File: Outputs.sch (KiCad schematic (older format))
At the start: 6 parts, among them Q7 MOSFET-N-SOT223

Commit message: Redesigned schematics and board
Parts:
- removed Q7: MOSFET-N-SOT223, symbol PIP-3104
- added Q7: VND14NV04, symbol MOSFET_N
- R53: renamed from R44; value 470 -> 2.4k
- renumbered D29 to D30, D30 to D31, D28 to D32, R43 to R54
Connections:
- net labels removed: FP-LED-5v
- wire segments 6 -> 9
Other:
- note added: "Fuel Pump Relay Output"
- moved on the sheet: D30, D31, D32, R53, R54
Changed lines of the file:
@@
-EESchema Schematic File Version 2  date Thu 19 Jan 2012 12:17:41 AM EST
+EESchema Schematic File Version 2  date Fri 20 Jan 2012 02:23:37 PM EST
 LIBS:power
 LIBS:device
@@
 Sheet 2 7
 Title "Outputs"
-Date "19 jan 2012"
+Date "20 jan 2012"
 Rev "A"
 Comp "Jaguar Board for FreeEMS"
@@
 Comment4 ""
 $EndDescr
-Connection ~ 7300 2000
 $Comp
-L DIODE D30
+L MOSFET_N Q7
+U 1 1 4F19BBF5
+P 6250 3500
+F 0 "Q7" H 6260 3670 60  0000 R CNN
+F 1 "VND14NV04" H 6260 3350 60  0000 R CNN
+	1    6250 3500
+	1    0    0    -1
+$EndComp
+Connection ~ 4700 2700
+Wire Wire Line
+	4700 3100 4700 2700
+Connection ~ 6500 3100
+Wire Wire Line
+	6000 3100 6500 3100
+Connection ~ 6000 3100
+Connection ~ 5600 3100
+Connection ~ 4700 3100
+Connection ~ 5200 3100
+Connection ~ 5250 3500
+Connection ~ 5750 3500
+Connection ~ 6050 3500
+Connection ~ 6350 3700
+Connection ~ 6350 3300
+Connection ~ 6500 3300
+Connection ~ 6500 2700
+Wire Wire Line
+	6350 3700 6350 3900
+Wire Wire Line
+	6350 3900 6250 3900
+Wire Wire Line
+	5750 3500 6050 3500
+Wire Wire Line
+	5250 3500 5100 3500
+Wire Wire Line
+	6350 3300 6650 3300
+Wire Wire Line
+	6500 3100 6500 3300
+Wire Wire Line
+	4600 2700 6650 2700
+Text Notes 5500 4300 0    40   ~ 0
+Fuel Pump Relay Output
+$Comp
+L DIODE D31
 U 1 1 4F1784DB
-P 7100 2000
-F 0 "D30" H 7100 2100 40  0000 C CNN
-F 1 "1N4148" H 7100 1900 40  0000 C CNN
-	1    7100 2000
+P 5800 3100
+F 0 "D31" H 5800 3200 40  0000 C CNN
+F 1 "1N4148" H 5800 3000 40  0000 C CNN
+	1    5800 3100
 	1    0    0    -1
 $EndComp
 $Comp
-L PIP-3104 Q7
-U 1 1 4F14621B
-P 3050 2450
-F 0 "Q7" H 3060 2620 60  0000 R CNN
-F 1 "MOSFET-N-SOT223" H 3060 2300 60  0000 R CNN
-	1    3050 2450
-	1    0    0    -1
-$EndComp
-Connection ~ 6900 2000
-Text HLabel 7300 2000 2    60   Output ~ 0
-Relay_Negative
-Text HLabel 6000 2000 0    40   Input ~ 0
-FP-LED-5v
-Connection ~ 6000 2000
-Connection ~ 6500 2000
-$Comp
-L LED D29
+L LED D30
 U 1 1 4F1384E1
-P 6700 2000
-F 0 "D29" H 6700 2100 50  0000 C CNN
-F 1 "LED" H 6700 1900 50  0000 C CNN
-	1    6700 2000
+P 5400 3100
+F 0 "D30" H 5400 3200 40  0000 C CNN
+F 1 "LED" H 5400 3000 40  0000 C CNN
+	1    5400 3100
 	1    0    0    -1
 $EndComp
 $Comp
-L R R44
+L R R53
 U 1 1 4F1384D7
-P 6250 2000
-F 0 "R44" V 6330 2000 50  0000 C CNN
-F 1 "470" V 6250 2000 50  0000 C CNN
-	1    6250 2000
+P 4950 3100
+F 0 "R53" V 5030 3100 40  0000 C CNN
+F 1 "2.4k" V 4950 3100 40  0000 C CNN
+	1    4950 3100
 	0    1    1    0
 $EndComp
-Connection ~ 2050 2450
-Connection ~ 2550 2450
-Connection ~ 2850 2450
-Connection ~ 3150 2650
-Connection ~ 3150 2250
-Connection ~ 3300 2250
-Connection ~ 3300 1850
-Wire Wire Line
-	3450 1850 3100 1850
-Wire Wire Line
-	3150 2650 3150 2850
-Wire Wire Line
-	3150 2850 3050 2850
-Wire Wire Line
-	2550 2450 2850 2450
-Wire Wire Line
-	2050 2450 1900 2450
-Wire Wire Line
-	3150 2250 3450 2250
-Text HLabel 1900 2450 0    60   Input ~ 0
+Text HLabel 5100 3500 0    40   Input ~ 0
 PA7
-Text HLabel 3050 2850 0    60   Input ~ 0
+Text HLabel 6250 3900 0    40   Input ~ 0
 GND
-Text HLabel 3450 2250 2    60   Output ~ 0
+Text HLabel 6650 3300 2    40   Output ~ 0
 Relay_Negative
-Text HLabel 3450 1850 2    60   Output ~ 0
+Text HLabel 6650 2700 2    40   Output ~ 0
 Relay_Positive
-Text HLabel 3100 1850 0    60   Input ~ 0
+Text HLabel 4600 2700 0    40   Input ~ 0
 12vdc-switched-relay
 $Comp
-L DIODE D28
+L DIODE D32
 U 1 1 4F074524
-P 3300 2050
-F 0 "D28" H 3300 2150 40  0000 C CNN
-F 1 "1N4004" H 3300 1950 40  0000 C CNN
-	1    3300 2050
+P 6500 2900
+F 0 "D32" H 6500 3000 40  0000 C CNN
+F 1 "1N4004" H 6500 2800 40  0000 C CNN
+	1    6500 2900
 	0    -1   -1   0
 $EndComp
 $Comp
-L R R43
+L R R54
 U 1 1 4F0744B6
-P 2300 2450
-F 0 "R43" V 2380 2450 50  0000 C CNN
-F 1 "1k" V 2300 2450 50  0000 C CNN
-	1    2300 2450
+P 5500 3500
+F 0 "R54" V 5580 3500 40  0000 C CNN
+F 1 "1k" V 5500 3500 40  0000 C CNN
+	1    5500 3500
 	0    1    1    0
 $EndComp

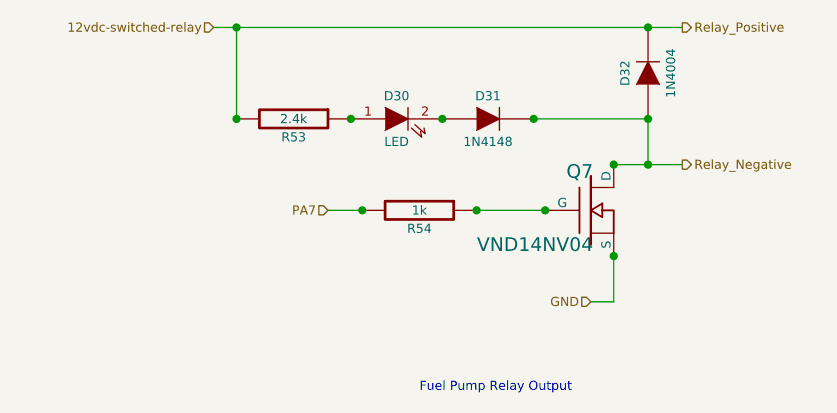
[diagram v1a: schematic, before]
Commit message: Updated Schematics, created new PDF, completed board layout and routing
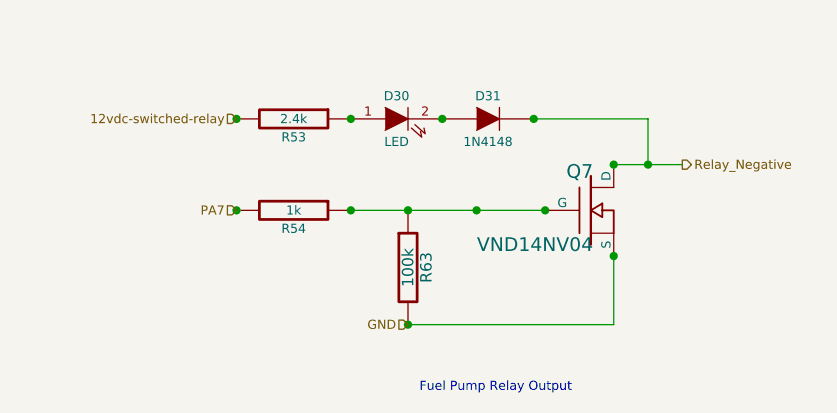
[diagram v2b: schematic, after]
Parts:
- removed D32: 1N4004, symbol DIODE
- added R63: 100k, symbol R
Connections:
- net GND: now also R63.2
- net at Q7.G, R54.1: now also R63.1
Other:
- moved on the sheet: R54
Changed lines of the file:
@@
-EESchema Schematic File Version 2  date Fri 20 Jan 2012 02:23:37 PM EST
+EESchema Schematic File Version 2  date Sun 22 Jan 2012 12:58:37 AM EST
 LIBS:power
 LIBS:device
@@
 Sheet 2 7
 Title "Outputs"
-Date "20 jan 2012"
+Date "22 jan 2012"
 Rev "A"
 Comp "Jaguar Board for FreeEMS"
@@
 Comment4 ""
 $EndDescr
+Connection ~ 4700 3500
+Connection ~ 5200 3500
+Connection ~ 5450 3500
+Connection ~ 5450 4000
+Wire Wire Line
+	6350 3700 6350 4000
+Wire Wire Line
+	6350 4000 5450 4000
+Wire Wire Line
+	5200 3500 6050 3500
+Wire Wire Line
+	6000 3100 6500 3100
+Connection ~ 6000 3100
+Connection ~ 5600 3100
+Connection ~ 4700 3100
+Connection ~ 5200 3100
+Connection ~ 5750 3500
+Connection ~ 6050 3500
+Connection ~ 6350 3700
+Connection ~ 6350 3300
+Connection ~ 6500 3300
+Wire Wire Line
+	6350 3300 6650 3300
+Wire Wire Line
+	6500 3100 6500 3300
+$Comp
+L R R63
+U 1 1 4F1AF0F6
+P 5450 3750
+F 0 "R63" V 5530 3750 50  0000 C CNN
+F 1 "100k" V 5450 3750 50  0000 C CNN
+	1    5450 3750
+	1    0    0    -1
+$EndComp
 $Comp
 L MOSFET_N Q7
@@
 	1    0    0    -1
 $EndComp
-Connection ~ 4700 2700
-Wire Wire Line
-	4700 3100 4700 2700
-Connection ~ 6500 3100
-Wire Wire Line
-	6000 3100 6500 3100
-Connection ~ 6000 3100
-Connection ~ 5600 3100
-Connection ~ 4700 3100
-Connection ~ 5200 3100
-Connection ~ 5250 3500
-Connection ~ 5750 3500
-Connection ~ 6050 3500
-Connection ~ 6350 3700
-Connection ~ 6350 3300
-Connection ~ 6500 3300
-Connection ~ 6500 2700
-Wire Wire Line
-	6350 3700 6350 3900
-Wire Wire Line
-	6350 3900 6250 3900
-Wire Wire Line
-	5750 3500 6050 3500
-Wire Wire Line
-	5250 3500 5100 3500
-Wire Wire Line
-	6350 3300 6650 3300
-Wire Wire Line
-	6500 3100 6500 3300
-Wire Wire Line
-	4600 2700 6650 2700
 Text Notes 5500 4300 0    40   ~ 0
 Fuel Pump Relay Output
@@
 	0    1    1    0
 $EndComp
-Text HLabel 5100 3500 0    40   Input ~ 0
+Text HLabel 4700 3500 0    40   Input ~ 0
 PA7
-Text HLabel 6250 3900 0    40   Input ~ 0
+Text HLabel 5450 4000 0    40   Input ~ 0
 GND
 Text HLabel 6650 3300 2    40   Output ~ 0
 Relay_Negative
-Text HLabel 6650 2700 2    40   Output ~ 0
-Relay_Positive
-Text HLabel 4600 2700 0    40   Input ~ 0
+Text HLabel 4700 3100 0    40   Input ~ 0
 12vdc-switched-relay
-$Comp
-L DIODE D32
-U 1 1 4F074524
-P 6500 2900
-F 0 "D32" H 6500 3000 40  0000 C CNN
-F 1 "1N4004" H 6500 2800 40  0000 C CNN
-	1    6500 2900
-	0    -1   -1   0
-$EndComp
 $Comp
 L R R54
 U 1 1 4F0744B6
-P 5500 3500
-F 0 "R54" V 5580 3500 40  0000 C CNN
-F 1 "1k" V 5500 3500 40  0000 C CNN
-	1    5500 3500
+P 4950 3500
+F 0 "R54" V 5030 3500 40  0000 C CNN
+F 1 "1k" V 4950 3500 40  0000 C CNN
+	1    4950 3500
 	0    1    1    0
 $EndComp

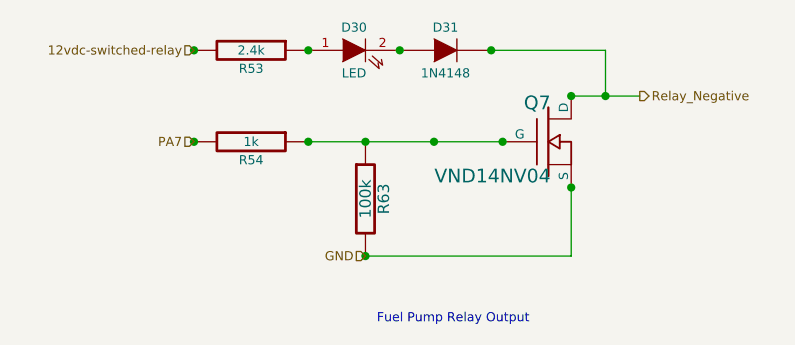
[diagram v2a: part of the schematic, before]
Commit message: Modified: schematics to correct errors
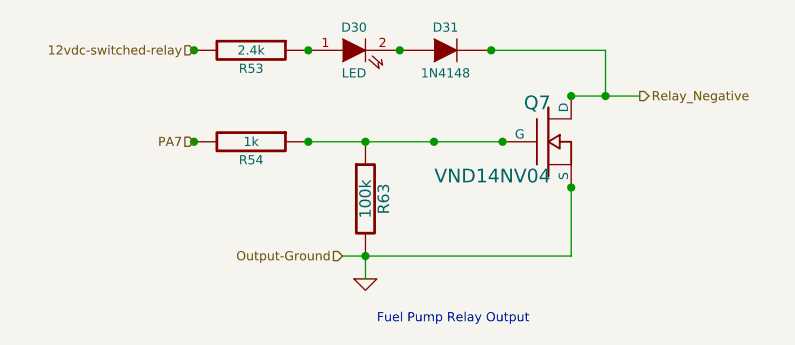
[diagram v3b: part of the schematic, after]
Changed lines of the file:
@@
-EESchema Schematic File Version 2  date Sun 22 Jan 2012 12:58:37 AM EST
+EESchema Schematic File Version 2  date Sun 22 Jan 2012 05:59:51 PM EST
 LIBS:power
 LIBS:device
@@
 Comment4 ""
 $EndDescr
-Connection ~ 4700 3500
-Connection ~ 5200 3500
-Connection ~ 5450 3500
-Connection ~ 5450 4000
+$Comp
+L GND #PWR56
+U 1 1 4F1C4528
+P 5450 4100
+F 0 "#PWR56" H 5450 4100 30  0001 C CNN
+F 1 "GND" H 5450 4030 30  0001 C CNN
+	1    5450 4100
+	1    0    0    -1
+$EndComp
 Wire Wire Line
-	6350 3700 6350 4000
+	5450 4100 5450 4000
 Wire Wire Line
-	6350 4000 5450 4000
+	6500 3300 6500 3100
+Wire Wire Line
+	6350 3300 6650 3300
+Connection ~ 6500 3300
+Connection ~ 6350 3300
+Connection ~ 6350 3700
+Connection ~ 6050 3500
+Connection ~ 5750 3500
+Connection ~ 5200 3100
+Connection ~ 4700 3100
+Connection ~ 5600 3100
+Connection ~ 6000 3100
+Wire Wire Line
+	6500 3100 6000 3100
 Wire Wire Line
 	5200 3500 6050 3500
 Wire Wire Line
-	6000 3100 6500 3100
-Connection ~ 6000 3100
-Connection ~ 5600 3100
-Connection ~ 4700 3100
-Connection ~ 5200 3100
-Connection ~ 5750 3500
-Connection ~ 6050 3500
-Connection ~ 6350 3700
-Connection ~ 6350 3300
-Connection ~ 6500 3300
+	6350 3700 6350 4000
+Connection ~ 5450 4000
+Connection ~ 5450 3500
+Connection ~ 5200 3500
+Connection ~ 4700 3500
 Wire Wire Line
-	6350 3300 6650 3300
-Wire Wire Line
-	6500 3100 6500 3300
+	6350 4000 5350 4000
+Text HLabel 5350 4000 0    40   Input ~ 0
+Output-Ground
 $Comp
 L R R63
@@
 Text HLabel 4700 3500 0    40   Input ~ 0
 PA7
-Text HLabel 5450 4000 0    40   Input ~ 0
-GND
 Text HLabel 6650 3300 2    40   Output ~ 0
 Relay_Negative

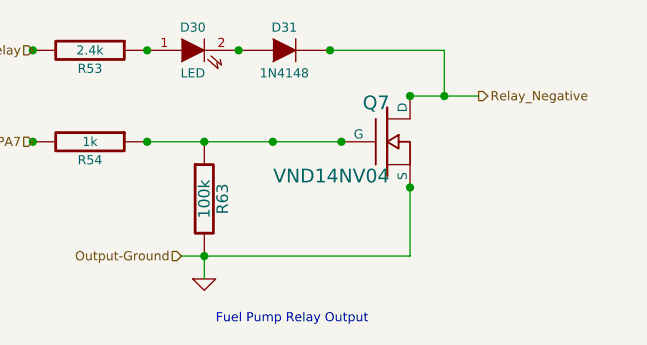
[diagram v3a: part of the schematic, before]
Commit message: Improved schematic, re-design board, re-created PDF
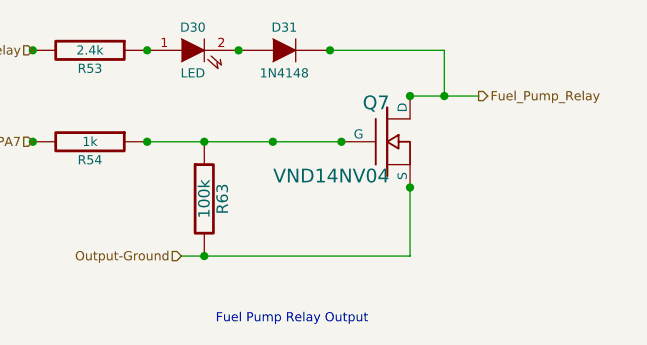
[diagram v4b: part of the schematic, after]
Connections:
- net GND renamed Output-Ground
- net Relay_Negative renamed Fuel_Pump_Relay
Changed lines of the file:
@@
-EESchema Schematic File Version 2  date Sun 22 Jan 2012 05:59:51 PM EST
+EESchema Schematic File Version 2  date Mon 23 Jan 2012 07:28:42 AM EST
 LIBS:power
 LIBS:device
@@
 EELAYER END
 $Descr A4 11700 8267
-Sheet 2 7
-Title "Outputs"
-Date "22 jan 2012"
-Rev "A"
-Comp "Jaguar Board for FreeEMS"
+Sheet 3 7
+Title "Jaguar PCB for FreeEMS"
+Date "23 jan 2012"
+Rev "A.1"
+Comp "diyefi.org"
 Comment1 ""
 Comment2 ""
@@
 Comment4 ""
 $EndDescr
-$Comp
-L GND #PWR56
-U 1 1 4F1C4528
-P 5450 4100
-F 0 "#PWR56" H 5450 4100 30  0001 C CNN
-F 1 "GND" H 5450 4030 30  0001 C CNN
-	1    5450 4100
-	1    0    0    -1
-$EndComp
 Wire Wire Line
-	5450 4100 5450 4000
+	5350 4000 6350 4000
+Connection ~ 4700 3500
+Connection ~ 5200 3500
+Connection ~ 5450 3500
+Connection ~ 5450 4000
 Wire Wire Line
-	6500 3300 6500 3100
-Wire Wire Line
-	6350 3300 6650 3300
-Connection ~ 6500 3300
-Connection ~ 6350 3300
-Connection ~ 6350 3700
-Connection ~ 6050 3500
-Connection ~ 5750 3500
-Connection ~ 5200 3100
-Connection ~ 4700 3100
-Connection ~ 5600 3100
-Connection ~ 6000 3100
-Wire Wire Line
-	6500 3100 6000 3100
+	6350 4000 6350 3700
 Wire Wire Line
 	5200 3500 6050 3500
 Wire Wire Line
-	6350 3700 6350 4000
-Connection ~ 5450 4000
-Connection ~ 5450 3500
-Connection ~ 5200 3500
-Connection ~ 4700 3500
+	6000 3100 6500 3100
+Connection ~ 6000 3100
+Connection ~ 5600 3100
+Connection ~ 4700 3100
+Connection ~ 5200 3100
+Connection ~ 5750 3500
+Connection ~ 6050 3500
+Connection ~ 6350 3700
+Connection ~ 6350 3300
+Connection ~ 6500 3300
 Wire Wire Line
-	6350 4000 5350 4000
+	6350 3300 6650 3300
+Wire Wire Line
+	6500 3100 6500 3300
 Text HLabel 5350 4000 0    40   Input ~ 0
 Output-Ground
@@
 PA7
 Text HLabel 6650 3300 2    40   Output ~ 0
-Relay_Negative
+Fuel_Pump_Relay
 Text HLabel 4700 3100 0    40   Input ~ 0
 12vdc-switched-relay
